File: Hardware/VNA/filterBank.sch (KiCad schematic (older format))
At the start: 18 parts, among them U10 74AHC1G04, U11 PE42440, U12 SN74LVC1G139, U13 PE42440

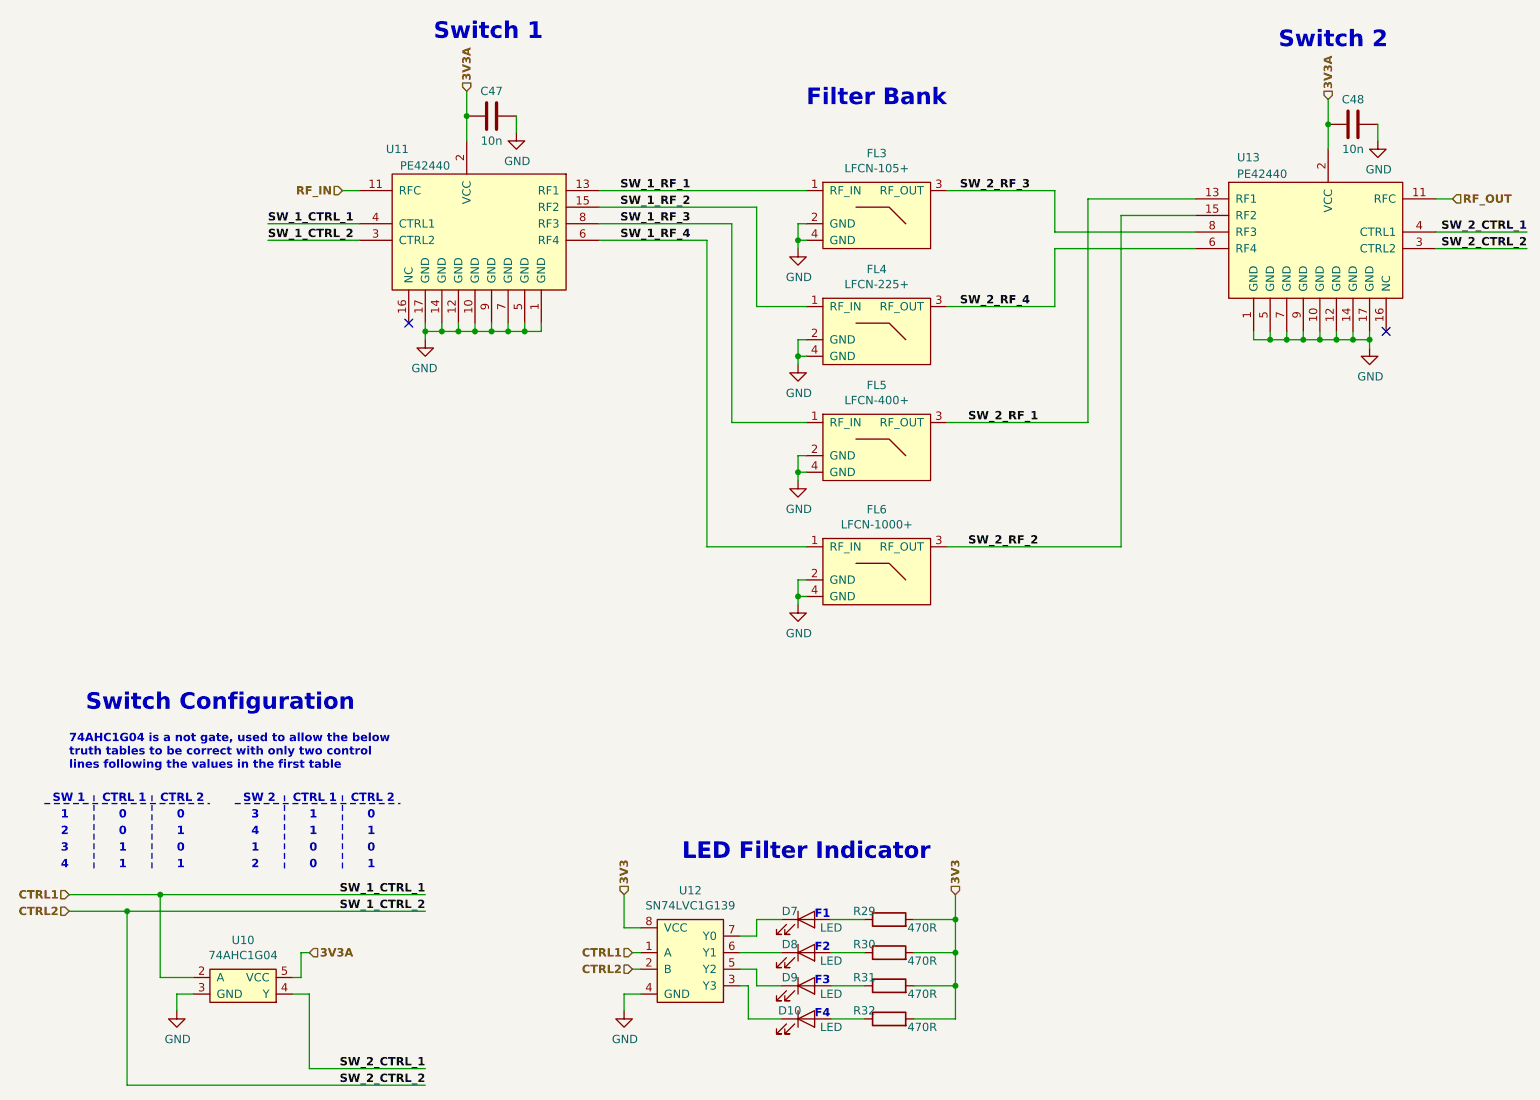
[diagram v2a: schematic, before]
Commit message: all 3d models created, prelim bom generated
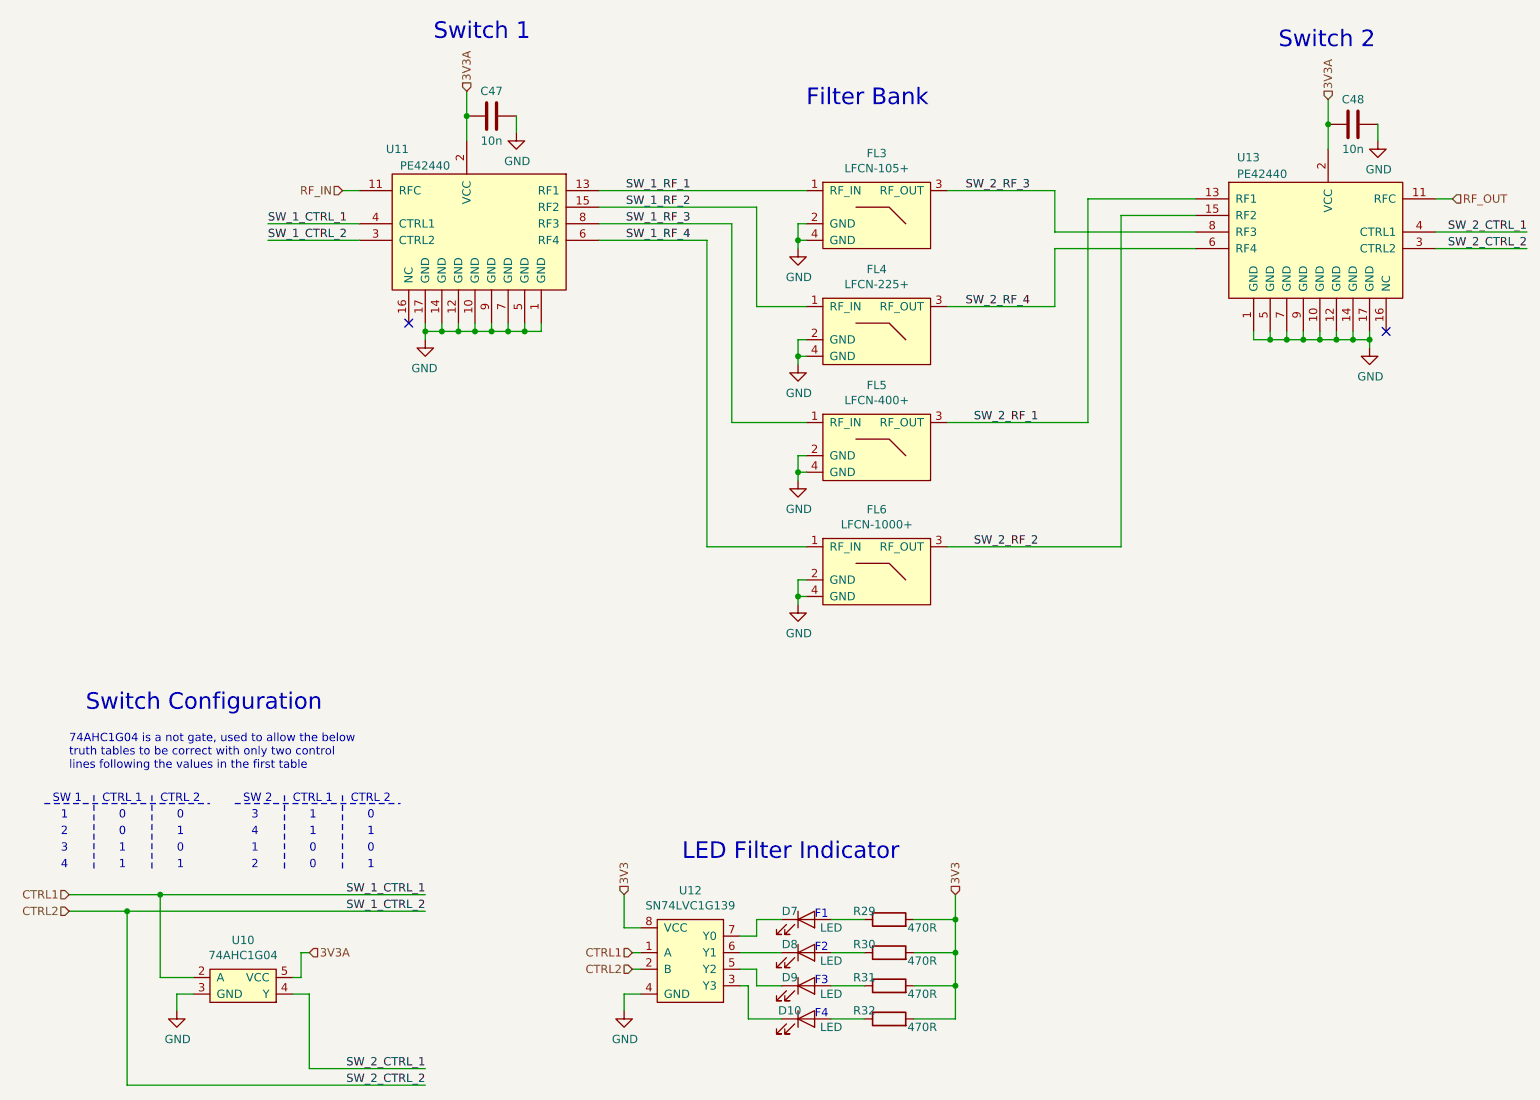
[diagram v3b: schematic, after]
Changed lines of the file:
@@
 	1    0    0    -1
 $EndComp
-Text Label 4600 2250 2    50   ~ 6
+Text Label 4600 2250 2    50   ~ 0
 SW_1_RF_1
-Text Label 4600 2350 2    50   ~ 6
+Text Label 4600 2350 2    50   ~ 0
 SW_1_RF_2
-Text Label 4600 2450 2    50   ~ 6
+Text Label 4600 2450 2    50   ~ 0
 SW_1_RF_3
-Text Label 4600 2550 2    50   ~ 6
+Text Label 4600 2550 2    50   ~ 0
 SW_1_RF_4
-Text Label 6650 2250 2    50   ~ 6
+Text Label 6650 2250 2    50   ~ 0
 SW_2_RF_3
-Text Label 6650 2950 2    50   ~ 6
+Text Label 6650 2950 2    50   ~ 0
 SW_2_RF_4
 $Comp
@@
 	1    0    0    -1
 $EndComp
-Text Label 3000 6500 2    50   ~ 6
+Text Label 3000 6500 2    50   ~ 0
 SW_1_CTRL_1
 Wire Wire Line
@@
 	1    0    0    -1
 $EndComp
-Text Label 3000 7550 2    50   ~ 6
+Text Label 3000 7550 2    50   ~ 0
 SW_2_CTRL_1
-Text Label 3000 6600 2    50   ~ 6
+Text Label 3000 6600 2    50   ~ 0
 SW_1_CTRL_2
 Wire Wire Line
@@
 Wire Wire Line
 	1200 7650 3000 7650
-Text Label 3000 7650 2    50   ~ 6
+Text Label 3000 7650 2    50   ~ 0
 SW_2_CTRL_2
-Text Notes 750  5950 0    50   ~ 6
+Text Notes 750  5950 0    50   ~ 0
 SW 1
-Text Notes 800  6050 0    50   ~ 6
-1
-Text Notes 800  6150 0    50   ~ 6
+Text Notes 800  6050 0    50   ~ 0
+1
+Text Notes 800  6150 0    50   ~ 0
 2
-Text Notes 800  6250 0    50   ~ 6
+Text Notes 800  6250 0    50   ~ 0
 3
-Text Notes 800  6350 0    50   ~ 6
+Text Notes 800  6350 0    50   ~ 0
 4
-Text Notes 1050 5950 0    50   ~ 6
+Text Notes 1050 5950 0    50   ~ 0
 CTRL 1
-Text Notes 1400 5950 0    50   ~ 6
+Text Notes 1400 5950 0    50   ~ 0
 CTRL 2
 Wire Notes Line
@@
 Wire Notes Line
 	1350 5900 1350 6350
-Text Notes 1500 6050 0    50   ~ 6
-0
-Text Notes 1500 6250 0    50   ~ 6
-0
-Text Notes 1500 6150 0    50   ~ 6
-1
-Text Notes 1500 6350 0    50   ~ 6
-1
-Text Notes 1900 5950 0    50   ~ 6
+Text Notes 1500 6050 0    50   ~ 0
+0
+Text Notes 1500 6250 0    50   ~ 0
+0
+Text Notes 1500 6150 0    50   ~ 0
+1
+Text Notes 1500 6350 0    50   ~ 0
+1
+Text Notes 1900 5950 0    50   ~ 0
 SW 2
-Text Notes 1950 6250 0    50   ~ 6
-1
-Text Notes 1950 6350 0    50   ~ 6
+Text Notes 1950 6250 0    50   ~ 0
+1
+Text Notes 1950 6350 0    50   ~ 0
 2
-Text Notes 1950 6050 0    50   ~ 6
+Text Notes 1950 6050 0    50   ~ 0
 3
-Text Notes 1950 6150 0    50   ~ 6
+Text Notes 1950 6150 0    50   ~ 0
 4
-Text Notes 2200 5950 0    50   ~ 6
+Text Notes 2200 5950 0    50   ~ 0
 CTRL 1
-Text Notes 2550 5950 0    50   ~ 6
+Text Notes 2550 5950 0    50   ~ 0
 CTRL 2
 Wire Notes Line
@@
 Wire Notes Line
 	2500 5900 2500 6350
-Text Notes 2650 6050 0    50   ~ 6
-0
-Text Notes 2650 6250 0    50   ~ 6
-0
-Text Notes 2650 6150 0    50   ~ 6
-1
-Text Notes 2650 6350 0    50   ~ 6
+Text Notes 2650 6050 0    50   ~ 0
+0
+Text Notes 2650 6250 0    50   ~ 0
+0
+Text Notes 2650 6150 0    50   ~ 0
+1
+Text Notes 2650 6350 0    50   ~ 0
 1
 Wire Notes Line
@@
 Wire Notes Line
 	700  5950 1700 5950
-Text Notes 1150 6050 0    50   ~ 6
-0
-Text Notes 1150 6150 0    50   ~ 6
-0
-Text Notes 1150 6250 0    50   ~ 6
-1
-Text Notes 1150 6350 0    50   ~ 6
-1
-Text Notes 2300 6050 0    50   ~ 6
-1
-Text Notes 2300 6150 0    50   ~ 6
-1
-Text Notes 2300 6250 0    50   ~ 6
-0
-Text Notes 2300 6350 0    50   ~ 6
-0
-Text Notes 950  5400 0    100  ~ 6
+Text Notes 1150 6050 0    50   ~ 0
+0
+Text Notes 1150 6150 0    50   ~ 0
+0
+Text Notes 1150 6250 0    50   ~ 0
+1
+Text Notes 1150 6350 0    50   ~ 0
+1
+Text Notes 2300 6050 0    50   ~ 0
+1
+Text Notes 2300 6150 0    50   ~ 0
+1
+Text Notes 2300 6250 0    50   ~ 0
+0
+Text Notes 2300 6350 0    50   ~ 0
+0
+Text Notes 950  5400 0    100  ~ 0
 Switch Configuration\n
-Text Notes 850  5750 0    50   ~ 6
+Text Notes 850  5750 0    50   ~ 0
 74AHC1G04 is a not gate, used to allow the below \ntruth tables to be correct with only two control\nlines following the values in the first table
 Wire Wire Line
@@
 Wire Wire Line
 	1400 6500 3000 6500
-Text Label 6700 3650 2    50   ~ 6
+Text Label 6700 3650 2    50   ~ 0
 SW_2_RF_1
-Text Label 6700 4400 2    50   ~ 6
+Text Label 6700 4400 2    50   ~ 0
 SW_2_RF_2
 $Comp
@@
 Wire Wire Line
 	3250 1800 3250 1950
-Text Notes 5300 1750 0    100  ~ 6
+Text Notes 5300 1750 0    100  ~ 0
 Filter Bank
-Text Notes 3050 1350 0    100  ~ 6
+Text Notes 3050 1350 0    100  ~ 0
 Switch 1
-Text Notes 8150 1400 0    100  ~ 6
+Text Notes 8150 1400 0    100  ~ 0
 Switch 2
 Connection ~ 1200 6600
@@
 Wire Wire Line
 	1400 6500 850  6500
-Text HLabel 2500 2250 0    50   Input ~ 6
+Text HLabel 2500 2250 0    50   Input ~ 0
 RF_IN
-Text HLabel 9200 2300 2    50   Input ~ 6
+Text HLabel 9200 2300 2    50   Input ~ 0
 RF_OUT
-Text HLabel 850  6500 0    50   Input ~ 6
+Text HLabel 850  6500 0    50   Input ~ 0
 CTRL1
-Text HLabel 850  6600 0    50   Input ~ 6
+Text HLabel 850  6600 0    50   Input ~ 0
 CTRL2
 Wire Wire Line
@@
 Wire Wire Line
 	2600 2450 2050 2450
-Text Label 2050 2550 0    50   ~ 6
+Text Label 2050 2550 0    50   ~ 0
 SW_1_CTRL_2
-Text Label 2050 2450 0    50   ~ 6
+Text Label 2050 2450 0    50   ~ 0
 SW_1_CTRL_1
 $Comp
@@
 Wire Wire Line
 	9100 2500 9650 2500
-Text Label 9650 2600 2    50   ~ 6
+Text Label 9650 2600 2    50   ~ 0
 SW_2_CTRL_2
-Text Label 9650 2500 2    50   ~ 6
+Text Label 9650 2500 2    50   ~ 0
 SW_2_CTRL_1
 Wire Wire Line
@@
 Wire Wire Line
 	6150 4400 7200 4400
-Text HLabel 3250 1650 1    50   Input ~ 6
+Text HLabel 3250 1650 1    50   Input ~ 0
 3V3A
-Text HLabel 8450 1700 1    50   Input ~ 6
+Text HLabel 8450 1700 1    50   Input ~ 0
 3V3A
-Text HLabel 2300 6850 2    50   Input ~ 6
+Text HLabel 2300 6850 2    50   Input ~ 0
 3V3A
 Wire Wire Line
@@
 	1    0    0    -1
 $EndComp
-Text HLabel 4200 6500 1    50   Input ~ 6
+Text HLabel 4200 6500 1    50   Input ~ 0
 3V3
 Wire Wire Line
 	4200 6500 4200 6700
-Text HLabel 4250 6850 0    50   Input ~ 6
+Text HLabel 4250 6850 0    50   Input ~ 0
 CTRL1
-Text HLabel 4250 6950 0    50   Input ~ 6
+Text HLabel 4250 6950 0    50   Input ~ 0
 CTRL2
 Wire Wire Line
@@
 Wire Wire Line
 	6200 7050 6200 7250
-Text HLabel 6200 6500 1    50   Input ~ 6
+Text HLabel 6200 6500 1    50   Input ~ 0
 3V3
 Wire Wire Line
@@
 	0    -1   -1   0
 $EndComp
-Text Notes 5350 6650 0    50   ~ 6
+Text Notes 5350 6650 0    50   ~ 0
 F1
-Text Notes 5350 6850 0    50   ~ 6
+Text Notes 5350 6850 0    50   ~ 0
 F2
-Text Notes 5350 7050 0    50   ~ 6
+Text Notes 5350 7050 0    50   ~ 0
 F3
-Text Notes 5350 7250 0    50   ~ 6
+Text Notes 5350 7250 0    50   ~ 0
 F4
-Text Notes 4550 6300 0    100  ~ 6
+Text Notes 4550 6300 0    100  ~ 0
 LED Filter Indicator
 $EndSCHEMATC

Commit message: More schematic changes + updated functionals
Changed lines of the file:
@@
 	1    0    0    -1
 $EndComp
-Text Label 4600 2250 2    50   ~ 0
+Text Label 4600 2250 2    50   ~ 6
 SW_1_RF_1
-Text Label 4600 2350 2    50   ~ 0
+Text Label 4600 2350 2    50   ~ 6
 SW_1_RF_2
-Text Label 4600 2450 2    50   ~ 0
+Text Label 4600 2450 2    50   ~ 6
 SW_1_RF_3
-Text Label 4600 2550 2    50   ~ 0
+Text Label 4600 2550 2    50   ~ 6
 SW_1_RF_4
-Text Label 6650 2250 2    50   ~ 0
+Text Label 6650 2250 2    50   ~ 6
 SW_2_RF_3
-Text Label 6650 2950 2    50   ~ 0
+Text Label 6650 2950 2    50   ~ 6
 SW_2_RF_4
 $Comp
@@
 	1    0    0    -1
 $EndComp
-Text Label 3000 6500 2    50   ~ 0
+Text Label 3000 6500 2    50   ~ 6
 SW_1_CTRL_1
 Wire Wire Line
@@
 	1    0    0    -1
 $EndComp
-Text Label 3000 7550 2    50   ~ 0
+Text Label 3000 7550 2    50   ~ 6
 SW_2_CTRL_1
-Text Label 3000 6600 2    50   ~ 0
+Text Label 3000 6600 2    50   ~ 6
 SW_1_CTRL_2
 Wire Wire Line
@@
 Wire Wire Line
 	1200 7650 3000 7650
-Text Label 3000 7650 2    50   ~ 0
+Text Label 3000 7650 2    50   ~ 6
 SW_2_CTRL_2
-Text Notes 750  5950 0    50   ~ 0
+Text Notes 750  5950 0    50   ~ 6
 SW 1
-Text Notes 800  6050 0    50   ~ 0
-1
-Text Notes 800  6150 0    50   ~ 0
+Text Notes 800  6050 0    50   ~ 6
+1
+Text Notes 800  6150 0    50   ~ 6
 2
-Text Notes 800  6250 0    50   ~ 0
+Text Notes 800  6250 0    50   ~ 6
 3
-Text Notes 800  6350 0    50   ~ 0
+Text Notes 800  6350 0    50   ~ 6
 4
-Text Notes 1050 5950 0    50   ~ 0
+Text Notes 1050 5950 0    50   ~ 6
 CTRL 1
-Text Notes 1400 5950 0    50   ~ 0
+Text Notes 1400 5950 0    50   ~ 6
 CTRL 2
 Wire Notes Line
@@
 Wire Notes Line
 	1350 5900 1350 6350
-Text Notes 1500 6050 0    50   ~ 0
-0
-Text Notes 1500 6250 0    50   ~ 0
-0
-Text Notes 1500 6150 0    50   ~ 0
-1
-Text Notes 1500 6350 0    50   ~ 0
-1
-Text Notes 1900 5950 0    50   ~ 0
+Text Notes 1500 6050 0    50   ~ 6
+0
+Text Notes 1500 6250 0    50   ~ 6
+0
+Text Notes 1500 6150 0    50   ~ 6
+1
+Text Notes 1500 6350 0    50   ~ 6
+1
+Text Notes 1900 5950 0    50   ~ 6
 SW 2
-Text Notes 1950 6250 0    50   ~ 0
-1
-Text Notes 1950 6350 0    50   ~ 0
+Text Notes 1950 6250 0    50   ~ 6
+1
+Text Notes 1950 6350 0    50   ~ 6
 2
-Text Notes 1950 6050 0    50   ~ 0
+Text Notes 1950 6050 0    50   ~ 6
 3
-Text Notes 1950 6150 0    50   ~ 0
+Text Notes 1950 6150 0    50   ~ 6
 4
-Text Notes 2200 5950 0    50   ~ 0
+Text Notes 2200 5950 0    50   ~ 6
 CTRL 1
-Text Notes 2550 5950 0    50   ~ 0
+Text Notes 2550 5950 0    50   ~ 6
 CTRL 2
 Wire Notes Line
@@
 Wire Notes Line
 	2500 5900 2500 6350
-Text Notes 2650 6050 0    50   ~ 0
-0
-Text Notes 2650 6250 0    50   ~ 0
-0
-Text Notes 2650 6150 0    50   ~ 0
-1
-Text Notes 2650 6350 0    50   ~ 0
+Text Notes 2650 6050 0    50   ~ 6
+0
+Text Notes 2650 6250 0    50   ~ 6
+0
+Text Notes 2650 6150 0    50   ~ 6
+1
+Text Notes 2650 6350 0    50   ~ 6
 1
 Wire Notes Line
@@
 Wire Notes Line
 	700  5950 1700 5950
-Text Notes 1150 6050 0    50   ~ 0
-0
-Text Notes 1150 6150 0    50   ~ 0
-0
-Text Notes 1150 6250 0    50   ~ 0
-1
-Text Notes 1150 6350 0    50   ~ 0
-1
-Text Notes 2300 6050 0    50   ~ 0
-1
-Text Notes 2300 6150 0    50   ~ 0
-1
-Text Notes 2300 6250 0    50   ~ 0
-0
-Text Notes 2300 6350 0    50   ~ 0
-0
-Text Notes 950  5400 0    100  ~ 0
+Text Notes 1150 6050 0    50   ~ 6
+0
+Text Notes 1150 6150 0    50   ~ 6
+0
+Text Notes 1150 6250 0    50   ~ 6
+1
+Text Notes 1150 6350 0    50   ~ 6
+1
+Text Notes 2300 6050 0    50   ~ 6
+1
+Text Notes 2300 6150 0    50   ~ 6
+1
+Text Notes 2300 6250 0    50   ~ 6
+0
+Text Notes 2300 6350 0    50   ~ 6
+0
+Text Notes 950  5400 0    100  ~ 6
 Switch Configuration\n
-Text Notes 850  5750 0    50   ~ 0
+Text Notes 850  5750 0    50   ~ 6
 74AHC1G04 is a not gate, used to allow the below \ntruth tables to be correct with only two control\nlines following the values in the first table
 Wire Wire Line
@@
 Wire Wire Line
 	1400 6500 3000 6500
-Text Label 6700 3650 2    50   ~ 0
+Text Label 6700 3650 2    50   ~ 6
 SW_2_RF_1
-Text Label 6700 4400 2    50   ~ 0
+Text Label 6700 4400 2    50   ~ 6
 SW_2_RF_2
 $Comp
@@
 Wire Wire Line
 	3250 1800 3250 1950
-Text Notes 5300 1750 0    100  ~ 0
+Text Notes 5300 1750 0    100  ~ 6
 Filter Bank
-Text Notes 3050 1350 0    100  ~ 0
+Text Notes 3050 1350 0    100  ~ 6
 Switch 1
-Text Notes 8150 1400 0    100  ~ 0
+Text Notes 8150 1400 0    100  ~ 6
 Switch 2
 Connection ~ 1200 6600
@@
 Wire Wire Line
 	1400 6500 850  6500
-Text HLabel 2500 2250 0    50   Input ~ 0
+Text HLabel 2500 2250 0    50   Input ~ 6
 RF_IN
-Text HLabel 9200 2300 2    50   Input ~ 0
+Text HLabel 9200 2300 2    50   Input ~ 6
 RF_OUT
-Text HLabel 850  6500 0    50   Input ~ 0
+Text HLabel 850  6500 0    50   Input ~ 6
 CTRL1
-Text HLabel 850  6600 0    50   Input ~ 0
+Text HLabel 850  6600 0    50   Input ~ 6
 CTRL2
 Wire Wire Line
@@
 Wire Wire Line
 	2600 2450 2050 2450
-Text Label 2050 2550 0    50   ~ 0
+Text Label 2050 2550 0    50   ~ 6
 SW_1_CTRL_2
-Text Label 2050 2450 0    50   ~ 0
+Text Label 2050 2450 0    50   ~ 6
 SW_1_CTRL_1
 $Comp
@@
 Wire Wire Line
 	9100 2500 9650 2500
-Text Label 9650 2600 2    50   ~ 0
+Text Label 9650 2600 2    50   ~ 6
 SW_2_CTRL_2
-Text Label 9650 2500 2    50   ~ 0
+Text Label 9650 2500 2    50   ~ 6
 SW_2_CTRL_1
 Wire Wire Line
@@
 Wire Wire Line
 	6150 4400 7200 4400
-Text HLabel 3250 1650 1    50   Input ~ 0
+Text HLabel 3250 1650 1    50   Input ~ 6
 3V3A
-Text HLabel 8450 1700 1    50   Input ~ 0
+Text HLabel 8450 1700 1    50   Input ~ 6
 3V3A
-Text HLabel 2300 6850 2    50   Input ~ 0
+Text HLabel 2300 6850 2    50   Input ~ 6
 3V3A
 Wire Wire Line
@@
 	1    0    0    -1
 $EndComp
-Text HLabel 4200 6500 1    50   Input ~ 0
+Text HLabel 4200 6500 1    50   Input ~ 6
 3V3
 Wire Wire Line
 	4200 6500 4200 6700
-Text HLabel 4250 6850 0    50   Input ~ 0
+Text HLabel 4250 6850 0    50   Input ~ 6
 CTRL1
-Text HLabel 4250 6950 0    50   Input ~ 0
+Text HLabel 4250 6950 0    50   Input ~ 6
 CTRL2
 Wire Wire Line
@@
 Wire Wire Line
 	6200 7050 6200 7250
-Text HLabel 6200 6500 1    50   Input ~ 0
+Text HLabel 6200 6500 1    50   Input ~ 6
 3V3
 Wire Wire Line
@@
 	0    -1   -1   0
 $EndComp
-Text Notes 5350 6650 0    50   ~ 0
+Text Notes 5350 6650 0    50   ~ 6
 F1
-Text Notes 5350 6850 0    50   ~ 0
+Text Notes 5350 6850 0    50   ~ 6
 F2
-Text Notes 5350 7050 0    50   ~ 0
+Text Notes 5350 7050 0    50   ~ 6
 F3
-Text Notes 5350 7250 0    50   ~ 0
+Text Notes 5350 7250 0    50   ~ 6
 F4
-Text Notes 4550 6300 0    100  ~ 0
+Text Notes 4550 6300 0    100  ~ 6
 LED Filter Indicator
 $EndSCHEMATC
